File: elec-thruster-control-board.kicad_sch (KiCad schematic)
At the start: 51 parts, among them J1 gp8-pwm4A, J11 gp17-pwm0B, J12 gp2-pwm1A, J13 Conn_01x07, J15 gp6-pwm3A, J16 gp8-pwm4A, J18 gp19-pwm1B, J19 gp21-pwm2B, J2 gp0-pwm0A, J20 gp26-pwm5A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

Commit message: Ok heres the final final final final version mkay
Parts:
- added C1, C2: C, Capacitor_SMD:C_0805_2012Metric, symbol Device:C
- added R19, R20: R, Resistor_SMD:R_0805_2012Metric, symbol Device:R
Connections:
- net GND: now also R17.1, C1.2, C2.2; no longer R11.1
- net at D12.2 (A): now also R11.1; no longer R17.1
- net at J1.2 (Pin_2), R11.2, R17.2: now also C2.1, R20.2; no longer J13.6 (Pin_6), J4.20 (Pin_20)
- net at J3.2 (Pin_2), R12.2, R18.2: now also C1.1, R19.2; no longer J13.1 (Pin_1), J4.14 (Pin_14)
- new net: J13.1 (Pin_1), J4.14 (Pin_14), R19.1
- new net: J13.6 (Pin_6), J4.20 (Pin_20), R20.1
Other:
- moved on the sheet: R18

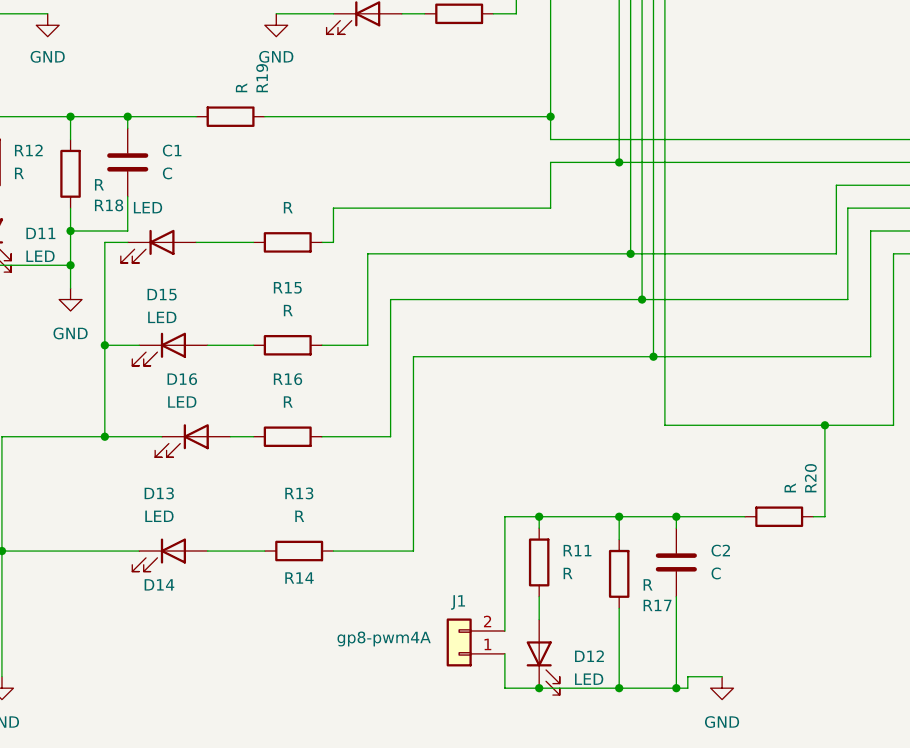
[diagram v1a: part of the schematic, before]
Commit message: Added Capacitor Values. Started BOM
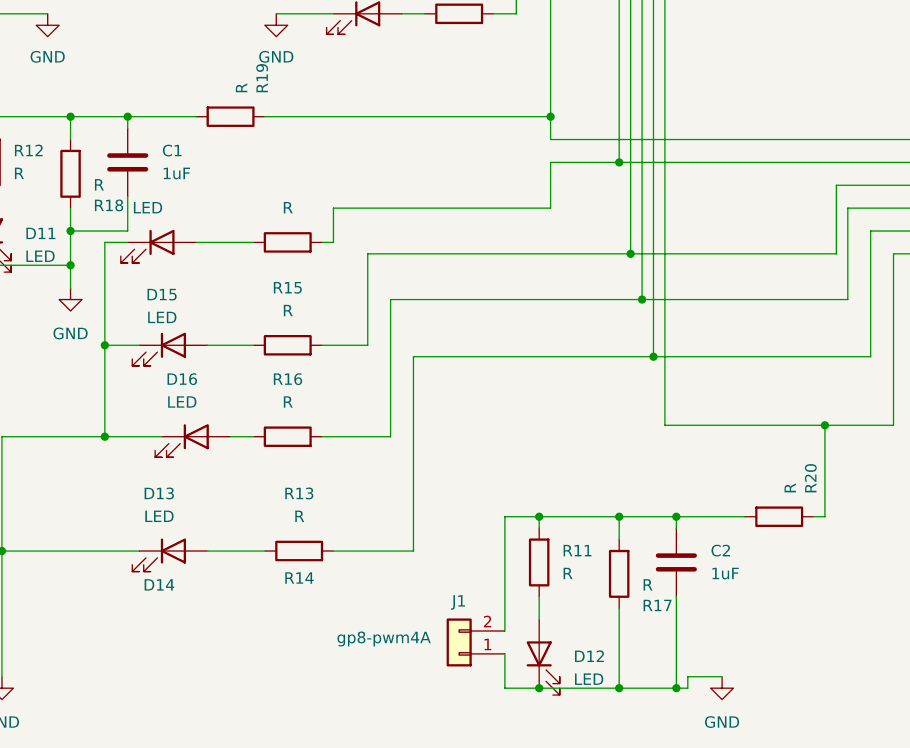
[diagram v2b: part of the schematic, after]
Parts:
- C1, C2: value C -> 1uF

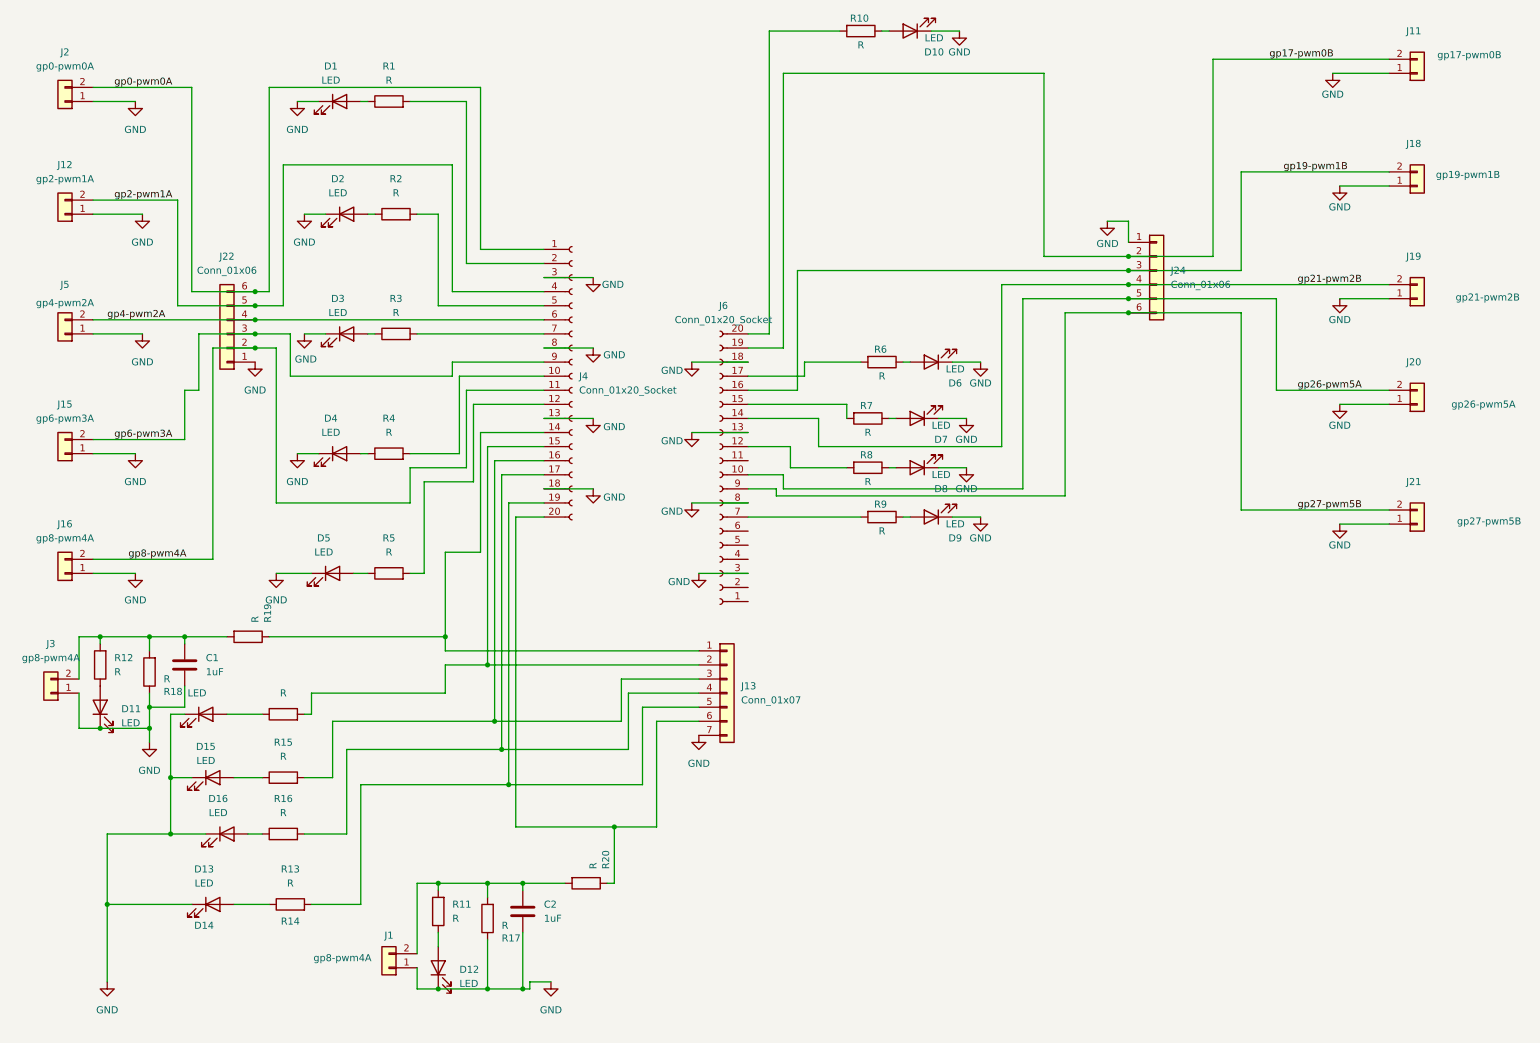
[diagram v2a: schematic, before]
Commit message: Completed BOM (and updated connector and resistors values to be correct)
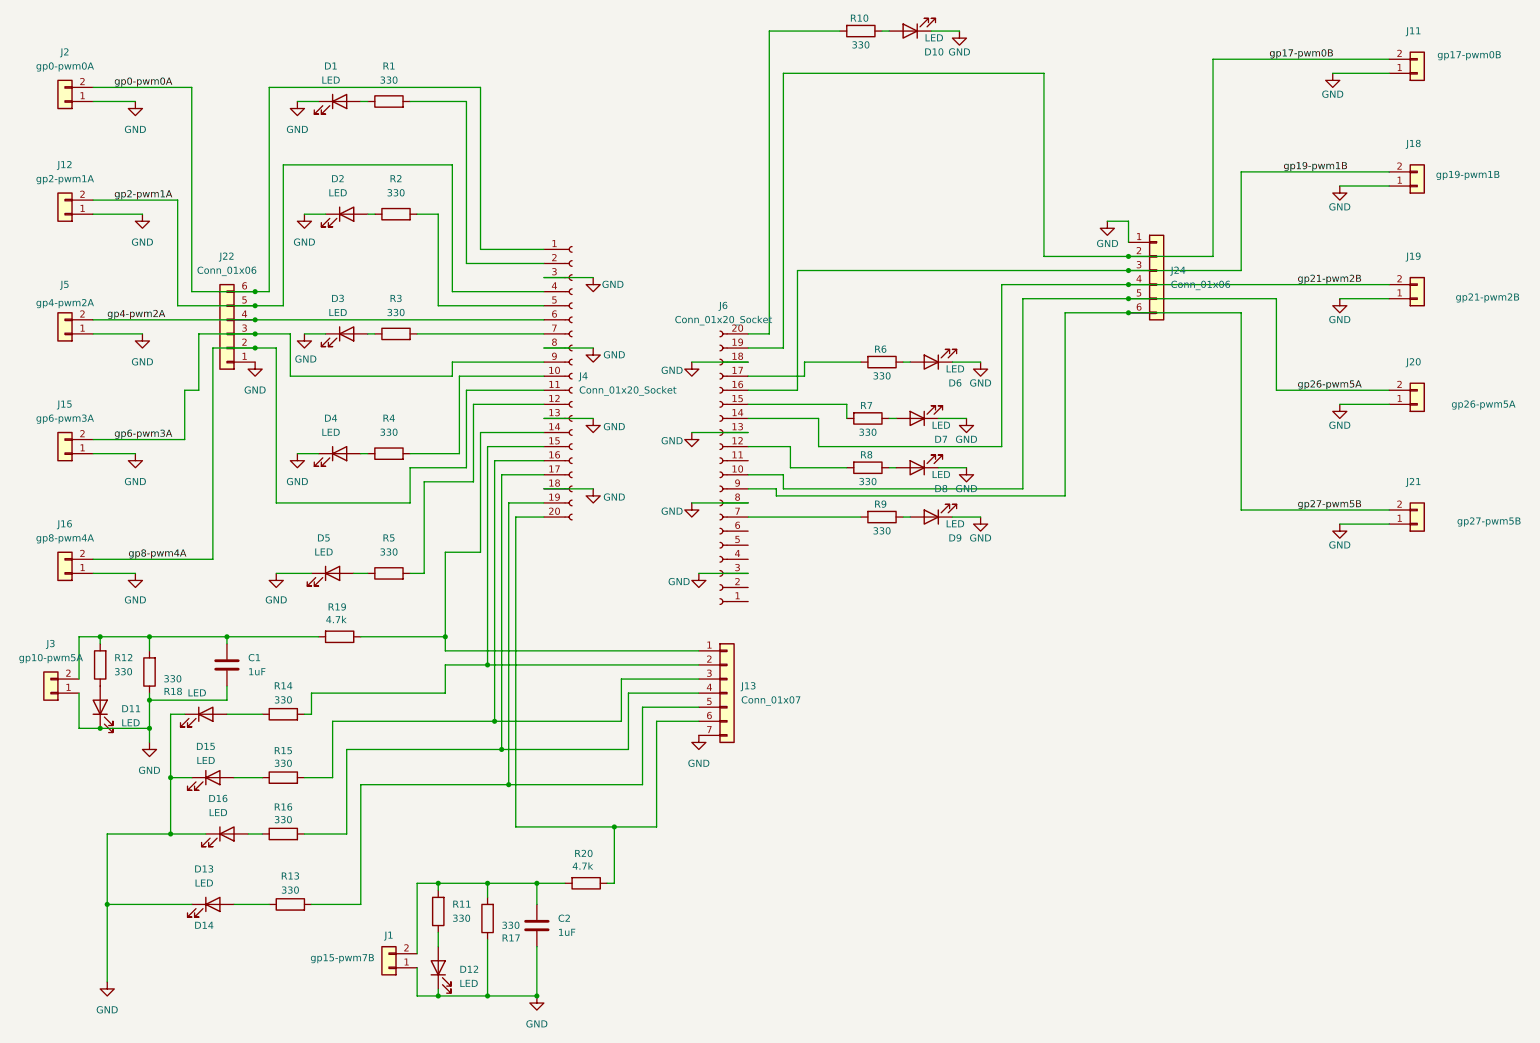
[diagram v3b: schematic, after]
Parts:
- C1, C2: Link (none) -> https://www.digikey.com/en/products/detail/cal-chip-electro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
- D1, D10, D11, D12, D13, D14, D15, D16, D2, D3, D4, D5, D6, D7, D8, D9: Link (none) -> https://www.digikey.com/en/products/detail/kingbright/APT20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; Notes (none) -> Green Color LED
- J1: value gp8-pwm4A -> gp15-pwm7B; Link (none) -> https://www.digikey.com/en/products/detail/jst-sales-americ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; Notes (none) -> Should already have
- J11, J12, J15, J16, J18, J19, J2, J20, J21, J5: Link (none) -> https://www.digikey.com/en/products/detail/jst-sales-americ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; Notes (none) -> Should already have
- J3: value gp8-pwm4A -> gp10-pwm5A; Link (none) -> https://www.digikey.com/en/products/detail/jst-sales-americ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; Notes (none) -> Should already have
- R1, R10, R11, R12, R13, R14, R15, R16, R17, R18, R2, R3, R4, R5, R6, R7, R8, R9: value R -> 330; footprint Resistor_SMD:R_0805_2012Metric -> RNCF0805DTE330R:RESC2012X65N; Link (none) -> https://www.digikey.com/en/products/detail/stackpole-electr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
- R19, R20: value R -> 4.7k; Link (none) -> https://www.digikey.com/en/products/detail/te-connectivity-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
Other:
- moved on the sheet: C1, C2, R19

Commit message: Final Draft of the Board (Hopefully Finalized) Updated all footprints to match parts in BOM Moved reference designators to proper locations (as importing new footprints moved them) Moved Kill switch connectors to have silkscreen labels more visible (no longer symmetrical, but there should be adequate spacing between parts
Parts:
- R19, R20: footprint Resistor_SMD:R_0805_2012Metric -> Imported Footprints:RESC2012X65N
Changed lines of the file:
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@@
 			)
 		)
-		(property "Footprint" "Resistor_SMD:R_0805_2012Metric"
+		(property "Footprint" "Imported Footprints:RESC2012X65N"
 			(at 113.03 172.212 90)
 			(effects
@@
 			)
 		)
-		(property "Footprint" "Resistor_SMD:R_0805_2012Metric"
+		(property "Footprint" "Imported Footprints:RESC2012X65N"
 			(at 68.58 127.762 90)
 			(effects

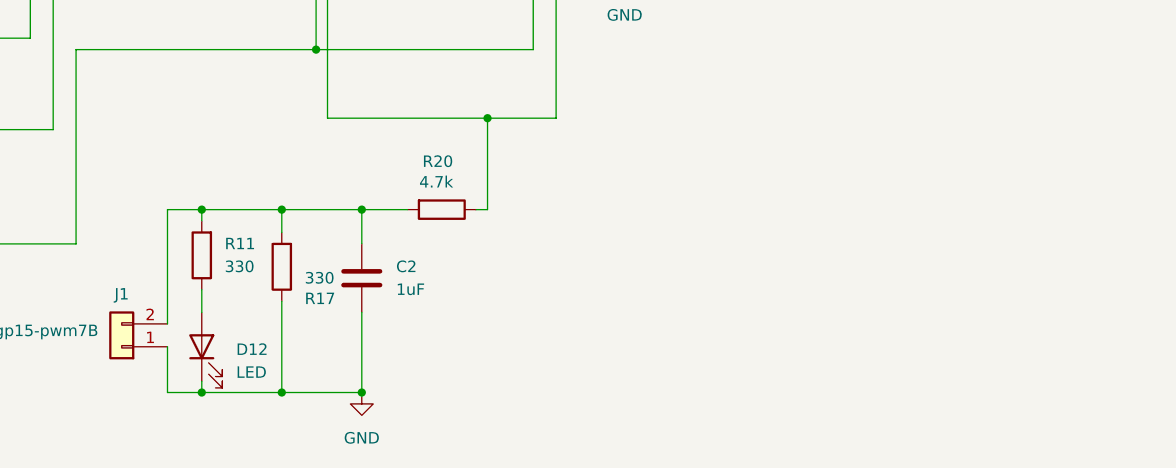
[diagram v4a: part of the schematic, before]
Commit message: Fixed resistor values
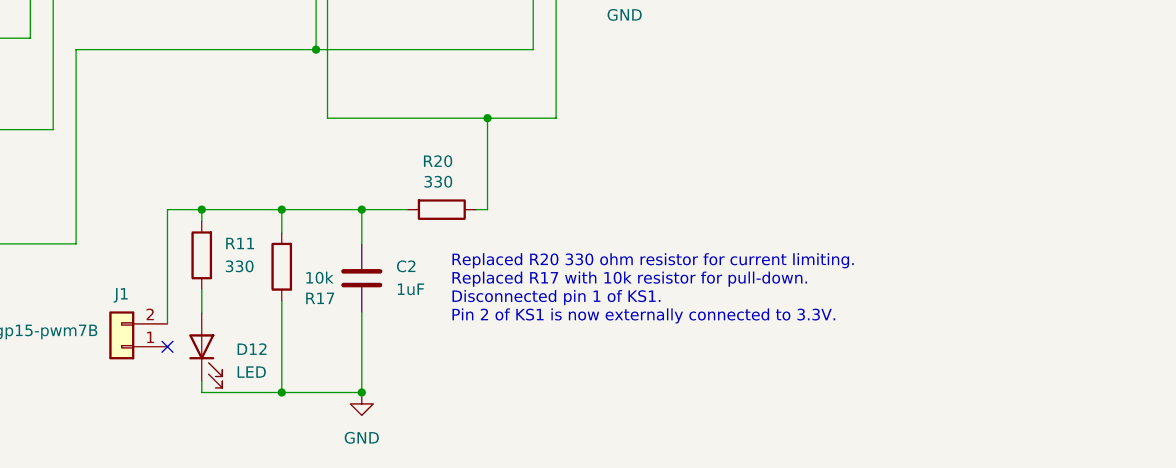
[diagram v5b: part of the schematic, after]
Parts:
- R17: value 330 -> 10k
- R20: value 4.7k -> 330
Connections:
- net GND: no longer J1.1 (Pin_1)
- no-connect marks 0 -> 1
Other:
- note added: "Replaced R20 330 ohm resistor for current limiting. Replaced R17 with 10k resistor for pull-down. Disconnected pin 1 of KS1. Pin 2 of KS1 is now externally connected to 3.3V."
